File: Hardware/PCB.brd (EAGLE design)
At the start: 46 x 35 mm, 105 parts, among them IC1 BQ25180YBGR, IC2 DRV2605YZFR, IC3 BMA421, IC9 RT6160AWSC, J1 503480-2400, J2 TC2030-IDC, J4 KH-TYPE-C-16P, Q1 20V/4.2A/52mΩ/1.4W, Q3 SI1308EDL-T1-GE3, U1 NRF52840_QF, U3 MAX17048G+T10, X1 32MHz, X2 32.768kHz

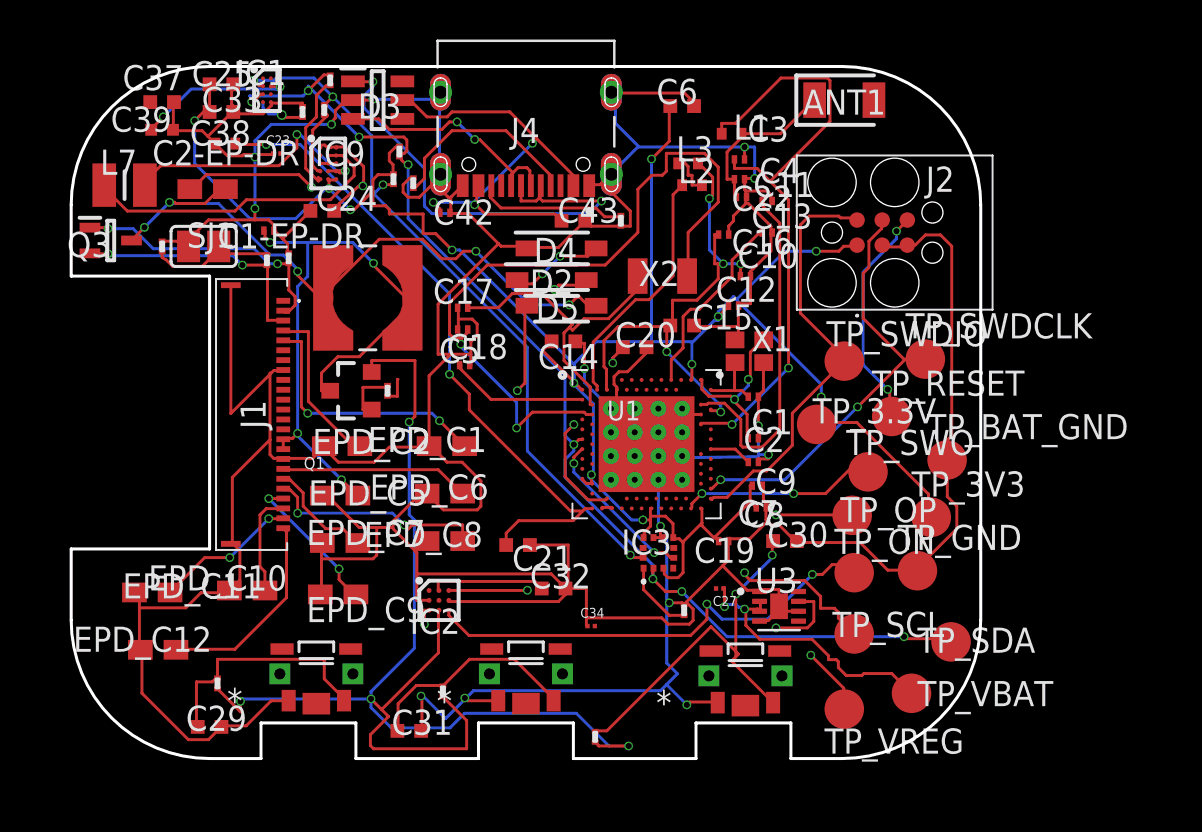
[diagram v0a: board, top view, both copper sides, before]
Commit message: pcb final
modificare rutare
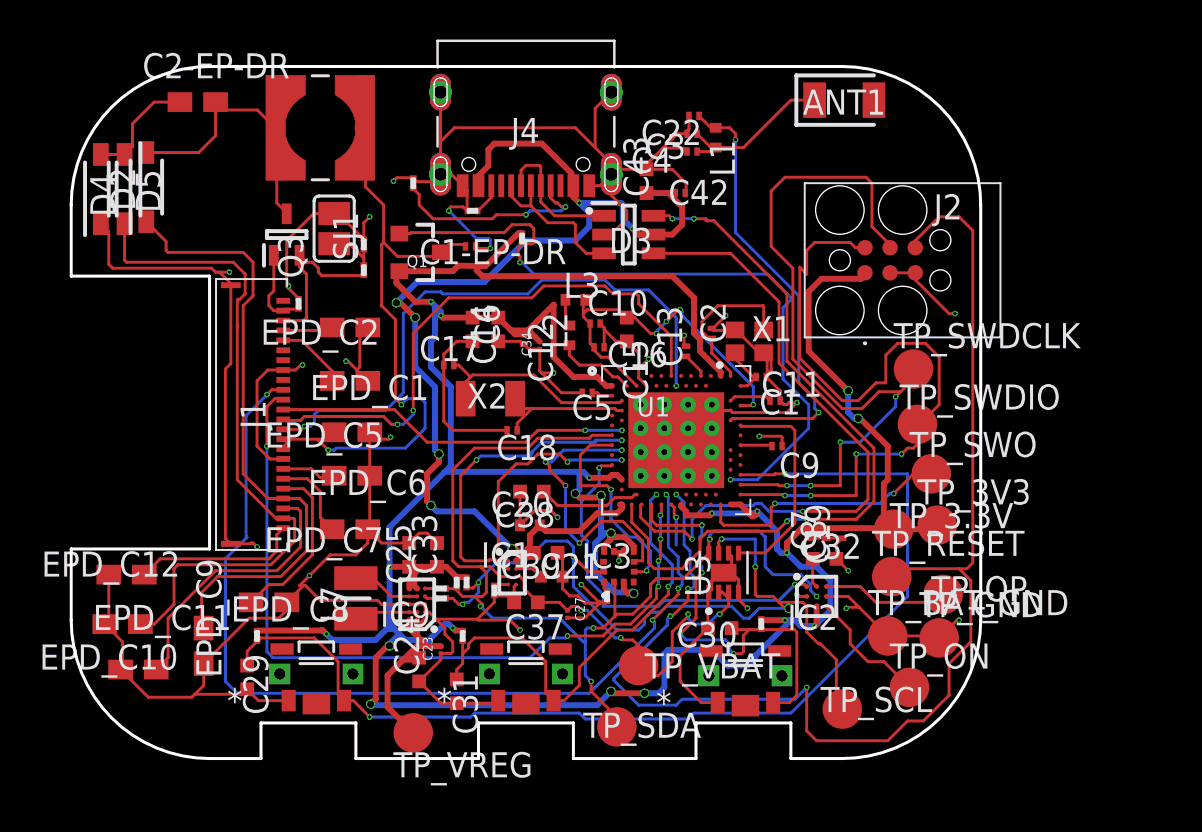
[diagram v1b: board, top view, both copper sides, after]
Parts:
- moved C37 31.3 mm to (-0.20, -10.2), turned to 180 degrees
- moved C39 30.0 mm to (1.10, -8.90)
- moved IC1 27.4 mm to (-0.90, -8.70)
- moved C23 26.4 mm to (-4.50, -12.6), turned to 90 degrees
- moved R2 26.3 mm to (-4.50, -9.50), turned to 270 degrees
- moved R9 26.1 mm to (-1.80, -9.60), turned to 180 degrees
- moved C25 25.6 mm to (-6.10, -7.80), turned to 90 degrees
- moved R4 25.4 mm to (-4.50, -10.0), turned to 270 degrees
- moved C33 24.9 mm to (-4.70, -7.80), turned to 90 degrees
- moved C38 24.7 mm to (0.00, -6.30)
- moved L7 24.0 mm to (-8.80, -10.0), turned to 90 degrees
- moved C24 23.7 mm to (-5.60, -13.6), turned to 90 degrees
- moved D4 23.5 mm to (-21.7, 10.7), turned to 90 degrees
- moved IC9 22.7 mm to (-5.70, -10.3), turned to 180 degrees
- moved D2 22.1 mm to (-20.5, 10.7), turned to 270 degrees
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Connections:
- net EPD_BUSY/1.5D renamed EPD_BUSY
- net EPS_BUSY/2.2D renamed EPS_BUSY
- removed net 3V3/1.7D: C34.2, IC2.C2, Q1.2, R5.2, R7.2, R8.2, R_PWR_EPD.2
- removed net 3V3/2.4A: C12.1, C14.1, C19.1, C25.1, C33.1, C6.1, C7.1, C8.1, IC3.10, IC3.3, IC3.7, IC9.E2, IC9.E3, J2.1, R17.1, R18.1, TP_3.3V.TP, TP_3V3.TP, U1.P$A22, U1.P$AD14, U1.P$AD23, U1.P$B1, U1.P$W1, U1.P$Y2
- removed net ALERT/1.6C: U3.5
- removed net ALERT/2.5C: U1.P$J24
- removed net D+/1.5D: D3.4
- removed net D-/1.5D: D3.6
- removed net D-/2.7D: U1.P$AD4, U1.P$AD6
- removed net EPD_CS.1.4C: J1.12
- removed net EPD_CS/2.2D: U1.P$K2
- removed net EPD_DC/1.5D: J1.11
- removed net EPD_DC/2.2D: U1.P$AD10
- removed net EPD_RST/1.5D: J1.10
- removed net EPD_RST/2.2D: U1.P$AC11
- removed net HAPTIC_EN/1.4C: IC2.A1
- removed net HAPTIC_EN/2.6A: U1.P$U1
- removed net MOSI/1.5B: J1.14
- removed net MOSI/2.2D: U1.P$B13
- removed net P0.13/1.5D: C30.1, R5.1, SW_UP.2
- removed net P0.13/2.6C: U1.P$AD8
- removed net P0.14/1.5D: C31.1, R8.1, SW_NET.2
- removed net P0.14/2.7C: U1.P$AC9
- removed net P1.01/1.6C: Q1.1, R_PWR_EPD.1
- removed net P1.01/2.4B: U1.P$Y23
- removed net P1.02/1.6C: C29.1, R7.1, SW_DN.2
- removed net P1.02/2.8C: U1.P$W24
- removed net SCK/1.5B: J1.13
- removed net SCK/2.2D: U1.P$A12
- removed net SCL/1.4C: IC2.C1, U3.7
- removed net SCL/2.4C: IC1.B1, IC3.12, R17.2, R4.1, TP_SCL.TP, U1.P$M2
- removed net SDA/1.4C: IC2.B2, U3.8
- removed net SDA/2.4C: IC1.C1, IC3.2, R18.2, R2.1, TP_SDA.TP, U1.P$L1
- removed net VBAT/1.2A: C27.2, TP_VBAT.TP, U3.2, U3.3
- removed net VBAT/2.5C: C37.1, IC1.C2
- removed net VBUS/1.5D: C42.1, C43.1, D3.5, J4.A4_B9, J4.A9_B4
- removed net VBUS/2.6D: C21.1, C38.2, IC1.A2, U1.P$AD2
- new net 3V3: C12.1, C14.1, C19.1, C25.1, C33.1, C34.2, C6.1, C7.1, C8.1, IC2.C2, IC3.10, IC3.3, IC3.7, IC9.E2, IC9.E3, J2.1, Q1.2, R17.1, R18.1, R5.2, R7.2, R8.2, R_PWR_EPD.2, TP_3.3V.TP, TP_3V3.TP, U1.P$A22, U1.P$AD14, U1.P$AD23, U1.P$B1, U1.P$W1, U1.P$Y2
- new net ALERT: U1.P$J24, U3.5
- new net D+: D3.4, U1.P$AD6
- new net D-: D3.6, U1.P$AD4
- new net EPD_CS: J1.12, U1.P$K2
- new net EPD_DC: J1.11, U1.P$AD10
- new net EPD_RST: J1.10, U1.P$AC11
- new net HAPTIC_EN: IC2.A1, U1.P$U1
- new net MOSI: J1.14, U1.P$B13
- new net P0.13: C30.1, R5.1, SW_UP.2, U1.P$AD8
- new net P0.14: C31.1, R8.1, SW_NET.2, U1.P$AC9
- new net P1.01: Q1.1, R_PWR_EPD.1, U1.P$Y23
- new net P1.02: C29.1, R7.1, SW_DN.2, U1.P$W24
- new net SCK: J1.13, U1.P$A12
- new net SCL: IC1.B1, IC2.C1, IC3.12, R17.2, R4.1, TP_SCL.TP, U1.P$M2, U3.7
- new net SDA: IC1.C1, IC2.B2, IC3.2, R18.2, R2.1, TP_SDA.TP, U1.P$L1, U3.8
- new net VBAT: C27.2, C37.1, IC1.C2, TP_VBAT.TP, U3.2, U3.3
- new net VBUS: C21.1, C38.2, C42.1, C43.1, D3.5, IC1.A2, J4.A4_B9, J4.A9_B4, U1.P$AD2
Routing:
- net 3V3: track 0.00 -> 173.5 mm, vias 0 -> 21
- net 3V3/2.4A: track 113.5 -> 0.00 mm, vias 12 -> 0
- net 3V3/1.7D: track 65.3 -> 0.00 mm, vias 4 -> 0
- net SDA/2.4C: track 57.7 -> 0.00 mm, vias 8 -> 0
- net SCL: track 0.00 -> 56.5 mm, vias 0 -> 9
- net VBUS: track 0.00 -> 56.3 mm, vias 0 -> 7
- net P1.02: track 0.00 -> 54.5 mm, vias 0 -> 2
- net RESET: track 11.5 -> 65.2 mm, vias 2 -> 4
- net SDA: track 0.00 -> 51.5 mm, vias 0 -> 5
- net SCL/2.4C: track 50.8 -> 0.00 mm, vias 5 -> 0
- net EPD_RST: track 0.00 -> 47.4 mm, vias 0 -> 4
- net EPD_DC: track 0.00 -> 39.3 mm, vias 0 -> 6
- net D-: track 0.00 -> 37.4 mm, vias 0 -> 4
- net P1.01: track 0.00 -> 36.3 mm, vias 0 -> 2
- net VREG: track 46.7 -> 11.3 mm, vias 2 -> 0
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- added copper zone on layer 2, net GND

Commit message: varianta finala
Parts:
- moved D5 2.00 mm to (-17.4, 10.8)
- moved D2 1.10 mm to (-19.4, 10.7)
- moved SW_DN 0.41 mm to (-11.2, -14.3), turned to 180 degrees
- moved SW_NET 0.22 mm to (-0.40, -14.3), turned to 180 degrees
- moved SW_UP 0.10 mm to (10.8, -14.3), turned to 180 degrees
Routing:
- net P0.13: track 22.7 -> 16.9 mm
- net GND: track 361.7 -> 365.6 mm, vias 27 -> 31
- net EPD_RST: track 47.4 -> 51.1 mm, vias 4 -> 6
- net P1.02: track 54.5 -> 58.0 mm
- net N$14: track 13.7 -> 11.7 mm
- net P0.14: track 23.6 -> 21.7 mm
- net 3V3: track 173.5 -> 175.2 mm
- net EPS_BUSY: track 2.21 -> 0.75 mm
- net PREVGL: track 34.3 -> 33.2 mm
- net VREG: track 11.3 -> 10.6 mm
- net PREVGH: track 31.6 -> 30.9 mm
- net N$15: track 5.77 -> 6.42 mm
